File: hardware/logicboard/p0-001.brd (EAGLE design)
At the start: 23 x 72 mm, 25 parts, among them IC1 74LS07N, IC2 LTC485N, IC3 LTC485N

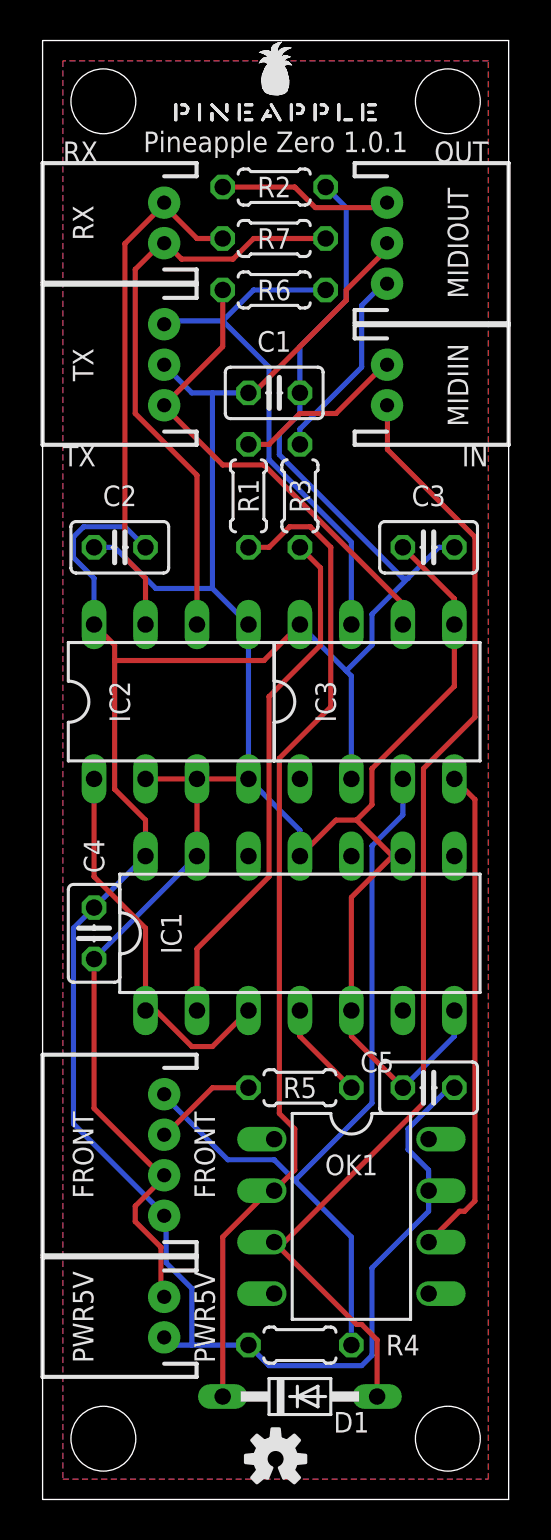
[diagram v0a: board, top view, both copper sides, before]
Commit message: Replaced D1.
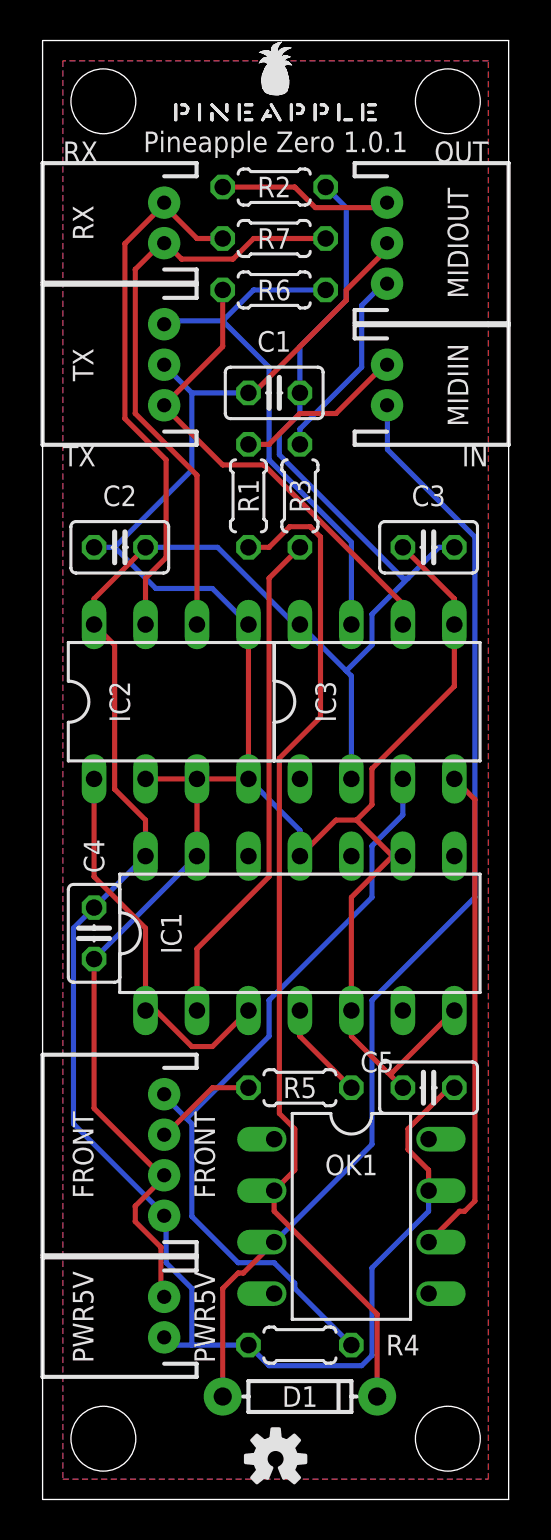
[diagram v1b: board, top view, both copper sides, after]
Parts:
- D1: value BAS15 -> (none); device diode:DO34-7 -> SparkFun-DiscreteSemi:DIODE-1N4148
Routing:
- net VCC: track 127.6 -> 122.8 mm
- net MIDIIN-: track 57.6 -> 56.0 mm
- net TXMUTE: track 39.6 -> 38.4 mm
- net RX-: track 25.7 -> 26.6 mm
- net N$2: track 25.8 -> 25.0 mm
- net GND: track 123.8 -> 123.0 mm

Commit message: Changed signal names.
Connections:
- net COM2 renamed MIDIIN
- net INDICATOR renamed INDR
- net N$15 renamed MIDIINA
- net N$2 renamed MIDIOUT-RAW
- net N$3 renamed IND
- net RX renamed MIDIOUT
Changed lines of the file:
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@@
 <wire x1="5.842" y1="14.224" x2="6" y2="14" width="0.254" layer="16"/>
 </signal>
-<signal name="N$2">
+<signal name="MIDIOUT-RAW">
 <contactref element="R3" pad="1"/>
 <contactref element="IC1" pad="2"/>
@@
 <wire x1="6.096" y1="54.102" x2="6" y2="54" width="0.254" layer="1"/>
 </signal>
-<signal name="N$15">
+<signal name="MIDIINA">
 <contactref element="D1" pad="C"/>
 <contactref element="R1" pad="1"/>
@@
 <wire x1="16.764" y1="55.88" x2="17" y2="56" width="0.254" layer="1"/>
 </signal>
-<signal name="COM2">
+<signal name="MIDIIN">
 <contactref element="OK1" pad="6"/>
 <contactref element="IC3" pad="4"/>
@@
 <wire x1="16.764" y1="63.754" x2="17" y2="64" width="0.254" layer="1"/>
 </signal>
-<signal name="RX">
+<signal name="MIDIOUT">
 <contactref element="IC2" pad="1"/>
 <contactref element="IC1" pad="1"/>
@@
 <wire x1="5.08" y1="24.13" x2="5.08" y2="28.194" width="0.254" layer="1"/>
 </signal>
-<signal name="N$3">
+<signal name="IND">
 <contactref element="IC1" pad="4"/>
 <contactref element="R5" pad="2"/>
@@
 <wire x1="15.24" y1="20.32" x2="12.7" y2="22.86" width="0.254" layer="1"/>
 </signal>
-<signal name="INDICATOR">
+<signal name="INDR">
 <contactref element="FRONT" pad="3"/>
 <contactref element="R5" pad="1"/>

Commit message: Version 1.0.1 -> 1.1.0.
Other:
- board text added: "Pineapple Zero 1.1.0"
- board text removed: "Pineapple Zero 1.0.1"
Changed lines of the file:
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@@
 <rectangle x1="0" y1="0" x2="23" y2="1" layer="42"/>
 <rectangle x1="0" y1="0" x2="1" y2="72" layer="42"/>
-<text x="11.5" y="67" size="1.016" layer="25" align="center">Pineapple Zero 1.0.1</text>
+<text x="11.5" y="67" size="1.016" layer="25" align="center">Pineapple Zero 1.1.0</text>
 </plain>
 <attributes>

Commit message: Pineapple Logo (vector->bitmap), OSHW logo (silk -> copper).
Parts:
- LOGO1: value OSHW-LOGOS -> OSHW-LOGOS-COPPER; device SparkFun-Aesthetics:OSHW-LOGO-S -> SparkFun-Aesthetics:OSHW-LOGO-S_COPPER
- U$1: value PINEAPPLELOGO2SILKMINI -> PINEAPPLE450; device pineapplelogo:PINEAPPLELOGO2SILKMINI -> pineapple:PINEAPPLE450
- moved U$1 1.00 mm to (11.5, 67.0)
- moved LOGO1 0.50 mm to (11.5, 2.50)
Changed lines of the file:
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@@
 <rectangle x1="0" y1="0" x2="23" y2="1" layer="42"/>
 <rectangle x1="0" y1="0" x2="1" y2="72" layer="42"/>
-<text x="11.5" y="67" size="1.016" layer="25" align="center">Pineapple Zero 1.1.0</text>
+<text x="11.5" y="2.5" size="1.016" layer="25" align="center">Pineapple Zero 1.1.0</text>
 </plain>
 <attributes>
@@
 <attribute name="VALUE" x="10.5664" y="5.3086" size="0.9906" layer="27" ratio="10"/>
 </element>
-<element name="LOGO1" library="SparkFun-Aesthetics" package="OSHW-LOGO-S" value="OSHW-LOGOS" x="11.5" y="2"/>
-<element name="U$1" library="pineapplelogo" package="PINEAPPLELOGO2SILKMINI" value="PINEAPPLELOGO2SILKMINI" x="11.5" y="68"/>
+<element name="LOGO1" library="SparkFun-Aesthetics" package="OSHW-LOGO-S_COPPER" value="OSHW-LOGOS-COPPER" x="11.5" y="2.5"/>
+<element name="U$1" library="pineapple" package="PINEAPPLE450" value="PINEAPPLE450" x="11.5" y="67"/>
 </elements>
 <signals>
